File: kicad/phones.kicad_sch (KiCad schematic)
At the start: 51 parts, among them J5 AudioJack3_Switch, SW13 RotaryEncoder, U14 OPA1656ID, U15 OPA1622

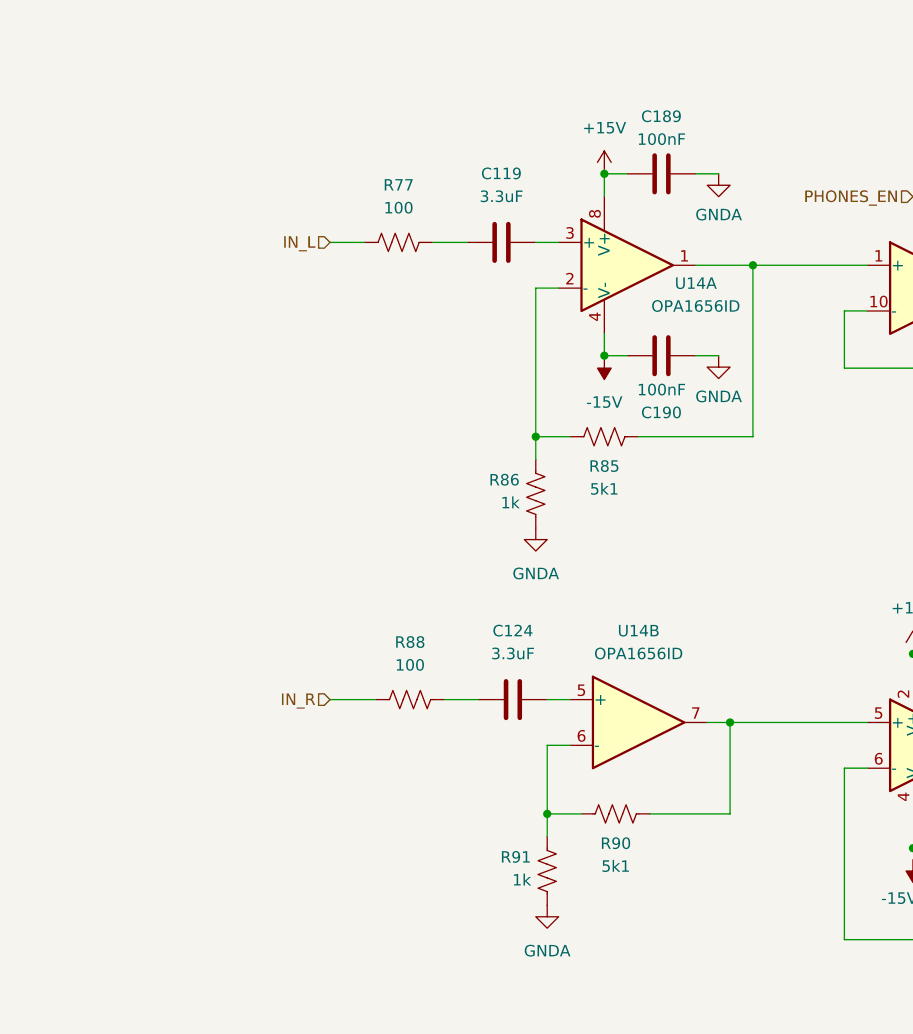
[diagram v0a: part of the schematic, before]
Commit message: output stage impedances
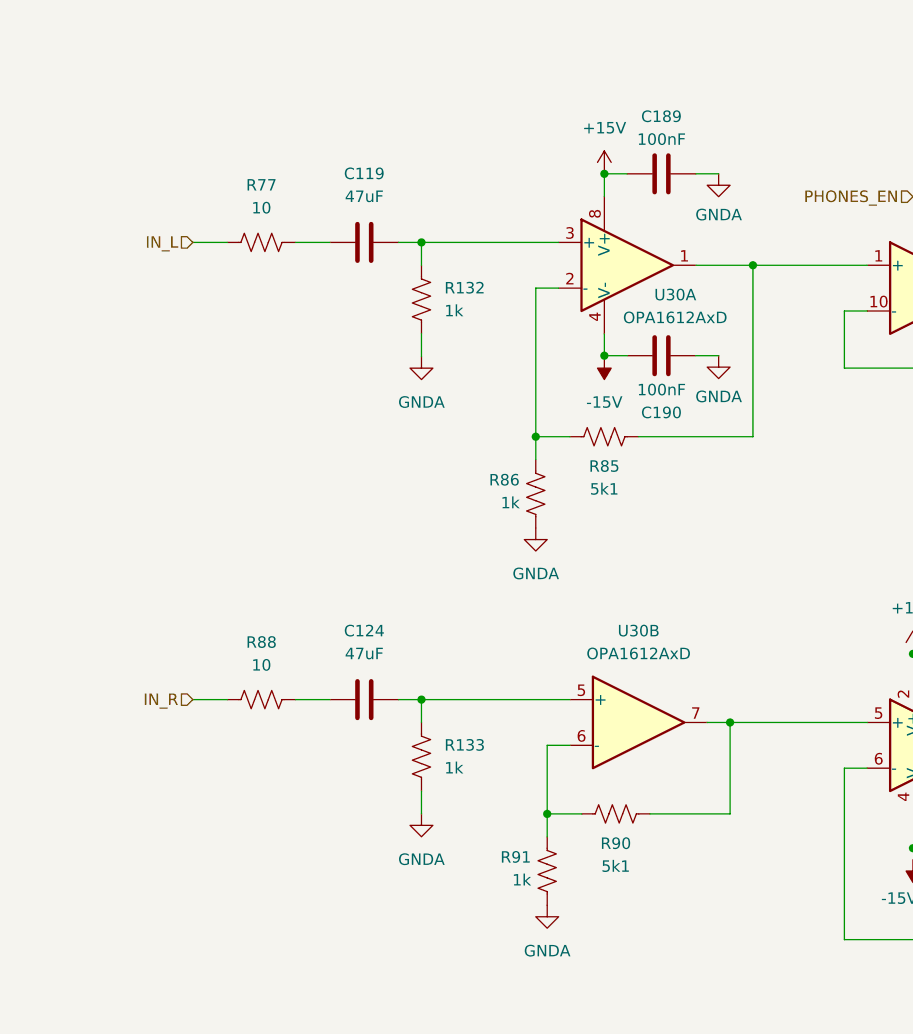
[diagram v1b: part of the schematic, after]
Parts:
- removed U14: OPA1656ID, Package_SO:SOIC-8_3.9x4.9mm_P1.27mm, symbol Amplifier_Operational:OPA1656ID
- added R132, R133: 1k, symbol Device:R_US
- added U30: OPA1612AxD, symbol Amplifier_Operational:OPA1612AxD
- C119, C124: value 3.3uF -> 47uF
- R77, R88: value 100 -> 10
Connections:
- net +15V: now also U30.8 (V+)
- net -15V: now also U30.4 (V-)
- net GNDA: now also R132.1, R133.1
- net at C124.2: now also R133.2, U30.5 (+)
- net at R90.2, R91.1: now also U30.6 (-)
- net at R90.1, U15.5 (+): now also U30.7
- net at C119.2: now also R132.2, U30.3 (+)
- net at R85.1, U15.1 (+): now also U30.1
- net at R85.2, R86.1: now also U30.2 (-)
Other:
- moved on the sheet: C119, R77

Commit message: #16
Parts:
- C120, C121: value 0.01uF -> 10nF
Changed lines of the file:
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@@
 			)
 		)
-		(property "Value" "0.01uF"
+		(property "Value" "10nF"
 			(at 241.3 106.6799 0)
 			(show_name no)
@@
 			)
 		)
-		(property "Value" "0.01uF"
+		(property "Value" "10nF"
 			(at 213.36 106.6799 0)
 			(show_name no)

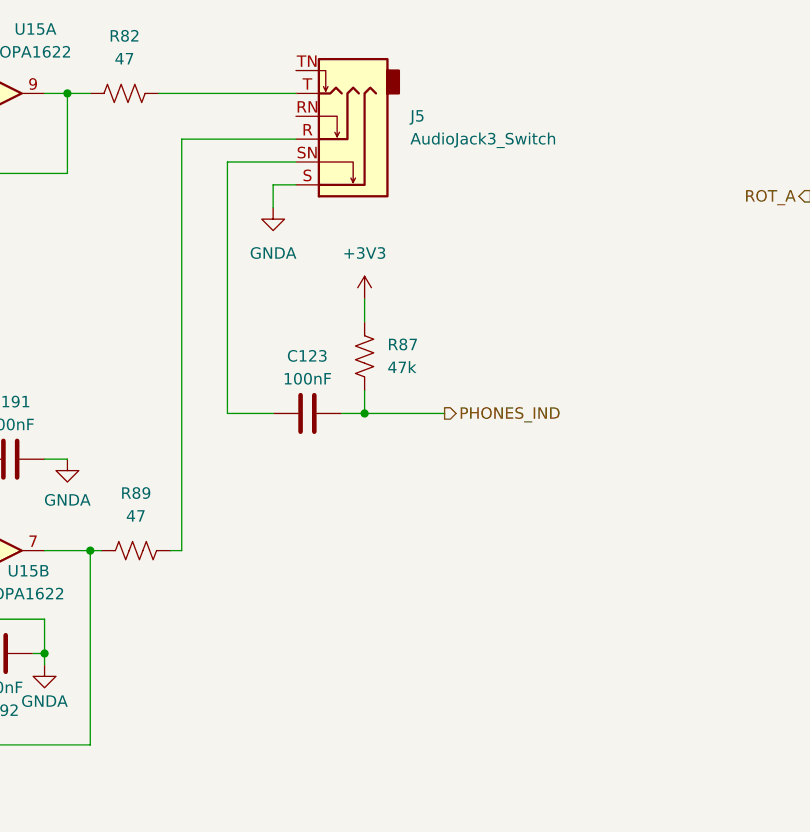
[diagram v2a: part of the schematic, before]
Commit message: push buttons
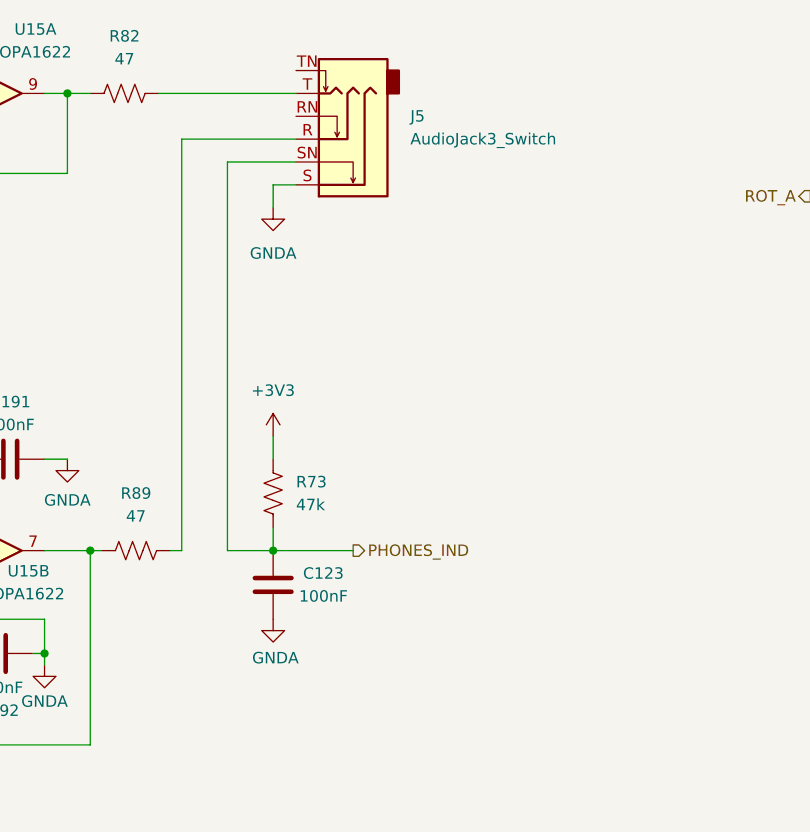
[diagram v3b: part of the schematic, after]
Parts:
- removed R87: 47k, symbol Device:R_US
- added R73: 47k, symbol Device:R_US
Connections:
- net +3V3: now also R73.1
- net GNDA: now also C123.2
- net PHONES_IND: now also C123.1, J5.SN, R73.2; no longer C123.2

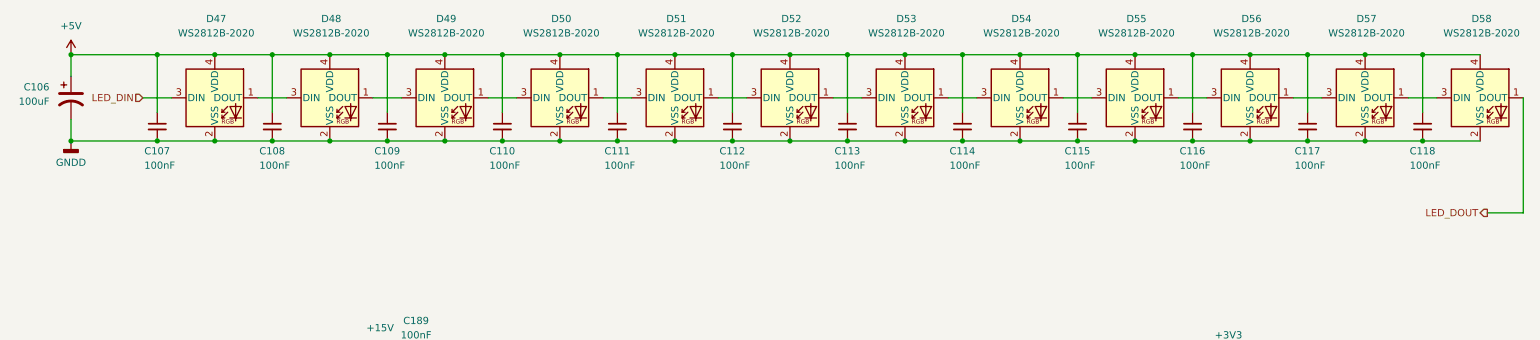
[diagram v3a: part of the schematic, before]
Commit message: reduced ws2812 count
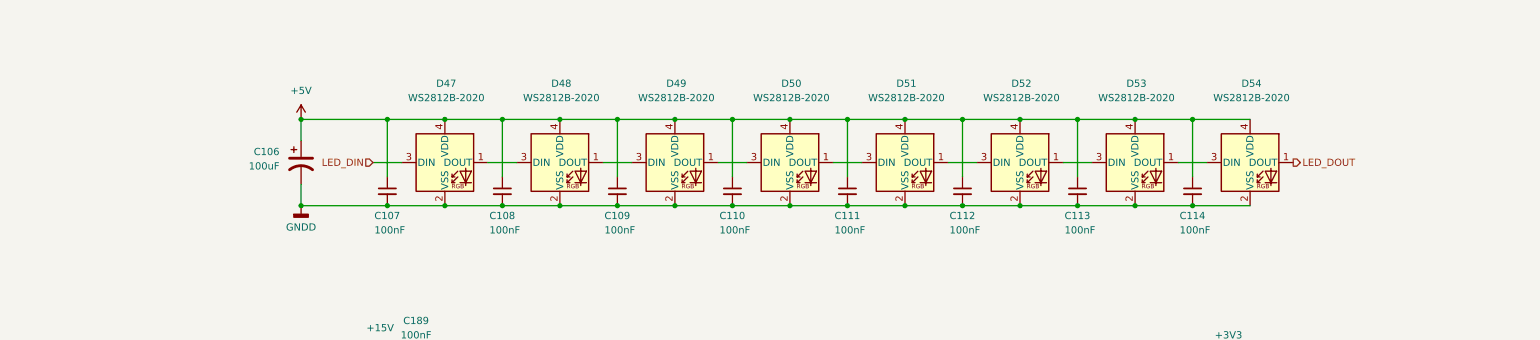
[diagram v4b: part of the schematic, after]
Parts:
- removed C115, C116, C117, C118: 100nF, symbol Device:C_Small
- removed D55, D56, D57, D58: WS2812B-2020, LED_SMD:LED_WS2812B-2020_PLCC4_2.0x2.0mm, symbol LED:WS2812B-2020
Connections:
- net LED_DOUT: now also D54.1 (DOUT)
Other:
- moved on the sheet: C106, C107, C108, C109, C110, C111, C112, C113, C114, D47, D48, D49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

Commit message: added footprints
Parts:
- SW13: footprint (none) -> openmic:PEC11L
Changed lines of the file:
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@@
 			)
 		)
-		(property "Footprint" ""
+		(property "Footprint" "openmic:PEC11L"
 			(at 223.266 95.25 0)
 			(hide yes)

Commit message: footprint selection
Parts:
- removed C106: 100uF, symbol Device:C_Polarized_US
- removed C119, C124: 47uF, symbol Device:C
- added C12: 100uF, Capacitor_SMD:CP_Elec_6.3x5.4, symbol Device:C_Polarized_US
- added C18, C27: 47uF, Capacitor_SMD:CP_Elec_6.3x5.4, symbol Device:C_Polarized_US
- C107, C108, C109, C110, C111, C112, C113, C114, C120, C121, C123, C189, C190, C191, C192: footprint (none) -> Capacitor_SMD:C_0603_1608Metric_Pad1.08x0.95mm_HandSolder
- R132, R133, R73, R77, R78, R79, R82, R83, R84, R85, R86, R88, R89, R90, R91: footprint (none) -> Resistor_SMD:R_0603_1608Metric_Pad0.98x0.95mm_HandSolder
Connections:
- net +5V: now also C12.1
- net GNDD: now also C12.2
- net at R77.2: now also C18.1
- net at R132.2, U30.3 (+): now also C18.2
- net at R133.2, U30.5 (+): now also C27.2
- net at R88.2: now also C27.1

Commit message: footprints
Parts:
- removed J5: AudioJack3_Switch, symbol Connector_Audio:AudioJack3_Switch
- added J8: NMJ6HHD2, Connector_Audio:Jack_6.35mm_Neutrik_NMJ6HHD2_Horizontal, symbol Connector_Audio:NMJ6HHD2
- U30: footprint (none) -> Package_SO:SOIC-8_3.9x4.9mm_P1.27mm
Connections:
- net GNDA: now also J8.S
- net PHONES_IND: now also J8.SN
- net at R82.2: now also J8.T
- net at R89.2: now also J8.R
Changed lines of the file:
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@@
 			)
 		)
-		(property "Footprint" ""
+		(property "Footprint" "Package_SO:SOIC-8_3.9x4.9mm_P1.27mm"
 			(at 80.01 85.09 0)
 			(hide yes)
@@
 			)
 		)
-		(property "Footprint" ""
+		(property "Footprint" "Package_SO:SOIC-8_3.9x4.9mm_P1.27mm"
 			(at 81.28 135.89 0)
 			(hide yes)
@@
 			)
 		)
-		(property "Footprint" ""
+		(property "Footprint" "Package_SO:SOIC-8_3.9x4.9mm_P1.27mm"
 			(at 80.01 85.09 0)
 			(hide yes)
@@
 	)
 	(symbol
-		(lib_id "Connector_Audio:AudioJack3_Switch")
-		(at 154.94 92.71 180)
-		(unit 1)
-		(body_style 1)
-		(exclude_from_sim no)
-		(in_bom yes)
-		(on_board yes)
-		(in_pos_files yes)
-		(dnp no)
-		(fields_autoplaced yes)
-		(property "Reference" "J5"
-			(at 162.56 90.1699 0)
-			(show_name no)
-			(do_not_autoplace no)
-			(effects
-				(font
-					(size 1.27 1.27)
-				)
-				(justify right)
-			)
-		)
-		(property "Value" "AudioJack3_Switch"
-			(at 162.56 92.7099 0)
-			(show_name no)
-			(do_not_autoplace no)
-			(effects
-				(font
-					(size 1.27 1.27)
-				)
-				(justify right)
-			)
-		)
-		(property "Footprint" ""
-			(at 154.94 92.71 0)
-			(hide yes)
-			(show_name no)
-			(do_not_autoplace no)
-			(effects
-				(font
-					(size 1.27 1.27)
-				)
-			)
-		)
-		(property "Datasheet" ""
-			(at 154.94 92.71 0)
-			(hide yes)
-			(show_name no)
-			(do_not_autoplace no)
-			(effects
-				(font
-					(size 1.27 1.27)
-				)
-			)
-		)
-		(property "Description" "Audio Jack, 3 Poles (Stereo / TRS), Switched Poles (Normalling)"
-			(at 154.94 92.71 0)
-			(hide yes)
-			(show_name no)
-			(do_not_autoplace no)
-			(effects
-				(font
-					(size 1.27 1.27)
-				)
-			)
-		)
-		(property "KLC_S3.3" ""
-			(at 154.94 92.71 0)
-			(hide yes)
-			(show_name no)
-			(do_not_autoplace no)
-			(effects
-				(font
-					(size 1.27 1.27)
-				)
-			)
-		)
-		(property "KLC_S4.1" ""
-			(at 154.94 92.71 0)
-			(hide yes)
-			(show_name no)
-			(do_not_autoplace no)
-			(effects
-				(font
-					(size 1.27 1.27)
-				)
-			)
-		)
-		(property "Sim.Type" ""
-			(at 154.94 92.71 0)
-			(hide yes)
-			(show_name no)
-			(do_not_autoplace no)
-			(effects
-				(font
-					(size 1.27 1.27)
-				)
-			)
-		)
-		(pin "SN"
-		)
-		(pin "S"
-		)
-		(pin "R"
-		)
-		(pin "TN"
-		)
-		(pin "T"
-		)
-		(pin "RN"
-		)
-		(instances
-			(project "openmic"
-				(path "/84faeadc-8b12-4a66-a17f-5c56e5923fb8/05cfbb15-a0d0-49ca-bcdf-c51b9947646b"
-					(reference "J5")
-					(unit 1)
-				)
-			)
-		)
-	)
-	(symbol
 		(lib_id "Device:R_US")
 		(at 243.84 99.06 90)
@@
 					(unit 1)
 				)
+			)
+		)
+	)
+	(symbol
+		(lib_id "Connector_Audio:NMJ6HHD2")
+		(at 154.94 92.71 180)
+		(unit 1)
+		(body_style 1)
+		(exclude_from_sim no)
+		(in_bom yes)
+		(on_board yes)
+		(in_pos_files yes)
+		(dnp no)
+		(fields_autoplaced yes)
+		(property "Reference" "J8"
+			(at 162.56 90.1699 0)
+			(show_name no)
+			(do_not_autoplace no)
+			(effects
+				(font
+					(size 1.27 1.27)
+				)
+				(justify right)
+			)
+		)
+		(property "Value" "NMJ6HHD2"
+			(at 162.56 92.7099 0)
+			(show_name no)
+			(do_not_autoplace no)
+			(effects
+				(font
+					(size 1.27 1.27)
+				)
+				(justify right)
+			)
+		)
+		(property "Footprint" "Connector_Audio:Jack_6.35mm_Neutrik_NMJ6HHD2_Horizontal"
+			(at 154.94 92.71 0)
+			(hide yes)
+			(show_name no)
+			(do_not_autoplace no)
+			(effects
+				(font
+					(size 1.27 1.27)
+				)
+			)
+		)
+		(property "Datasheet" "https://www.neutrik.com/en/product/nmj6hhd2"
+			(at 154.94 92.71 0)
+			(hide yes)
+			(show_name no)
+			(do_not_autoplace no)
+			(effects
+				(font
+					(size 1.27 1.27)
+				)
+			)
+		)
+		(property "Description" "M Series, 6.35mm (1/4in) stereo jack, switched, with half threaded nose and offset PCB pins"
+			(at 154.94 92.71 0)
+			(hide yes)
+			(show_name no)
+			(do_not_autoplace no)
+			(effects
+				(font
+					(size 1.27 1.27)
+				)
+			)
+		)
+		(pin "TN"
+		)
+		(pin "SN"
+		)
+		(pin "S"
+		)
+		(pin "T"
+		)
+		(pin "R"
+		)
+		(pin "RN"
+		)
+		(instances
+			(project "openmic"
+				(path "/84faeadc-8b12-4a66-a17f-5c56e5923fb8/05cfbb15-a0d0-49ca-bcdf-c51b9947646b"
+					(reference "J8")
+					(unit 1)
+				)

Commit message: output schematic pdfs
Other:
- note removed: "headphones out"
- company: (none) -> OpenMic
- title: (none) -> Headphones out
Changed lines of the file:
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@@
 	(generator "eeschema")
 	(generator_version "10.0")
-	(paper "A4")
-	(text "headphones out"
-		(exclude_from_sim no)
-		(at 217.805 175.895 0)
-		(effects
-			(font
-				(size 2.54 2.54)
-			)
-			(justify left bottom)
-		)
+	(paper "USLetter")
+	(title_block
+		(title "Headphones out")
+		(date "2026-05-15")
+		(company "OpenMic")
 	)
 	(junction
